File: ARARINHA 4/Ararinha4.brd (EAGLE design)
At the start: 160 x 100 mm, 105 parts, among them IC1 4053N, Q1 BC548, Q2 BC548, Q3 BC548, Q4 BC548, Q5 BC548, Q6 BC548, U1 LM386

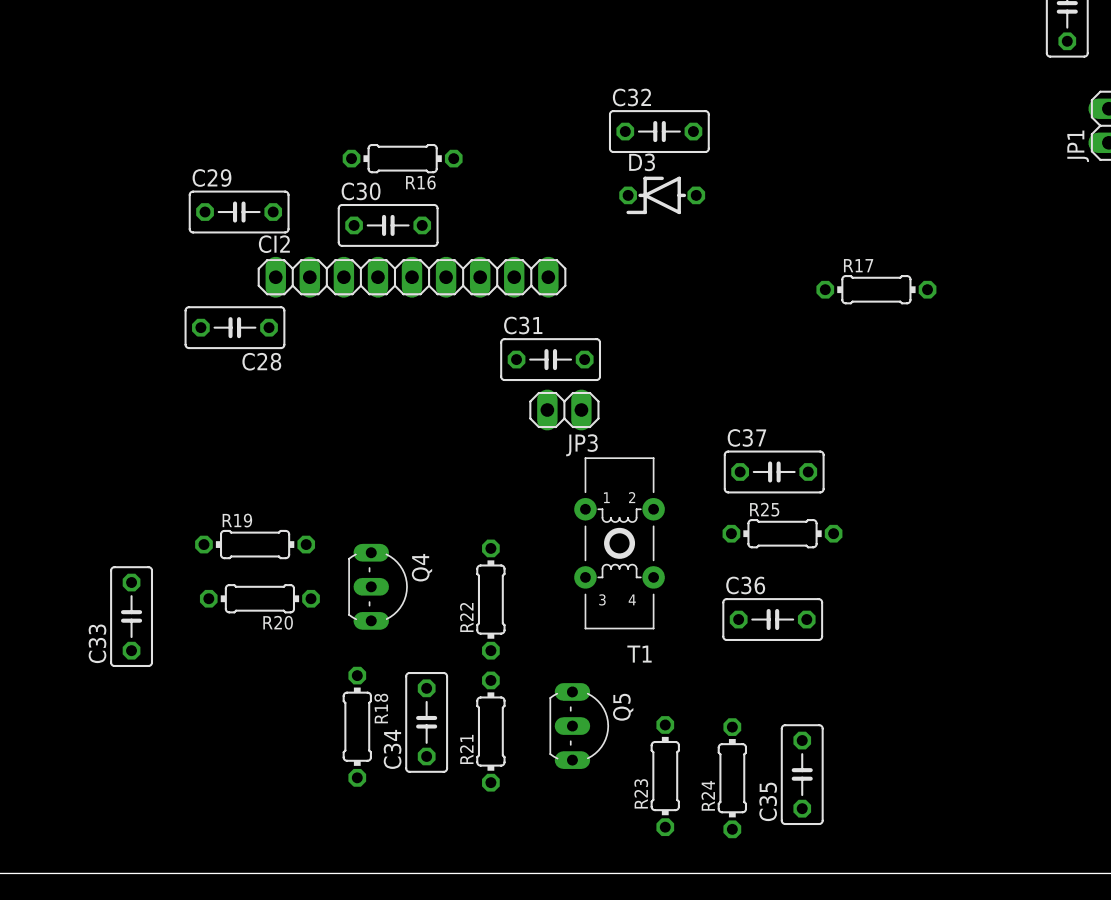
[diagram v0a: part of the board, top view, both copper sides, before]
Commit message: 
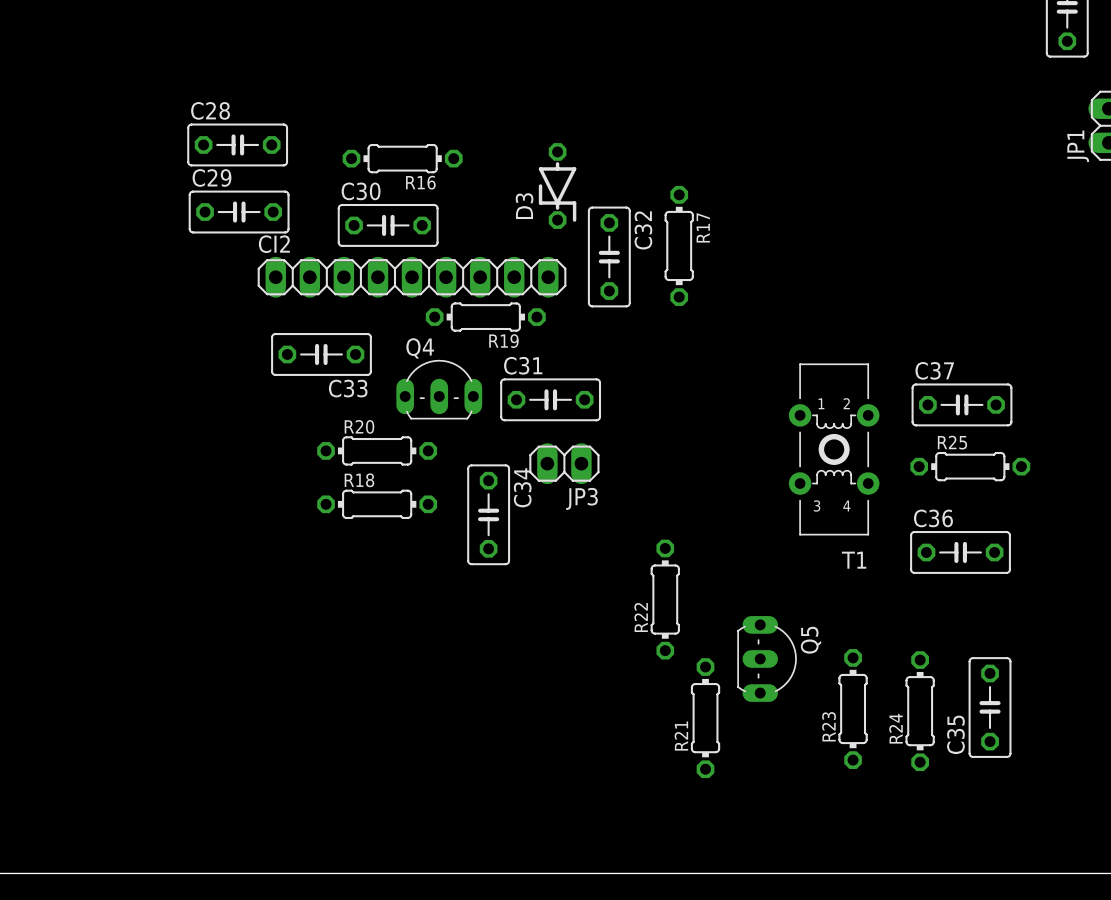
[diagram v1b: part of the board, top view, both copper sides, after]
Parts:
- moved R19 24.2 mm to (84.1, 41.5), turned to 180 degrees
- moved C33 24.1 mm to (71.8, 38.7), turned to 180 degrees
- moved T1 17.5 mm to (110.1, 31.6)
- moved R18 16.6 mm to (76.0, 27.5), turned to 0 degrees
- moved C34 16.2 mm to (84.3, 26.7), turned to 270 degrees
- moved R21 16.0 mm to (100.5, 11.6)
- moved Q4 15.9 mm to (80.6, 36.8), turned to 0 degrees
- moved R17 15.1 mm to (98.5, 46.8), turned to 270 degrees
- moved C35 14.9 mm to (121.7, 12.4)
- moved C36 14.9 mm to (119.5, 23.9)
- moved C37 14.9 mm to (119.6, 34.9)
- moved Q5 14.9 mm to (105.8, 16.0)
- moved R23 14.9 mm to (111.5, 12.3)
- moved R24 14.9 mm to (116.5, 12.1)
- moved R25 14.9 mm to (120.2, 30.3)
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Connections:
- net GND: now also C28.1, R18.1; no longer C28.2, R18.2
- net N$30: now also C28.2; no longer C28.1
- net N$41: now also R18.2; no longer R18.1
- net N$42: now also R20.2; no longer R20.1
- net N$44: now also R20.1; no longer R20.2

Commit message: 
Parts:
- added RXANT: TXOUT, pinhead:1X02
- moved T2 199.5 mm to (96.6, 30.8), turned to 270 degrees
- moved R30 183.5 mm to (102.0, 32.7), turned to 270 degrees
- moved R32 169.0 mm to (62.8, 26.0), turned to 270 degrees
- moved C16 167.1 mm to (68.4, 68.1), turned to 90 degrees
- moved C41 158.2 mm to (88.4, 22.7), turned to 270 degrees
- moved C40 157.9 mm to (96.8, 22.4), turned to 180 degrees
- moved R29 156.0 mm to (80.0, 28.3)
- moved JP5 148.4 mm to (104.7, 21.8), turned to 270 degrees
- moved R28 145.3 mm to (80.0, 32.0)
- moved Q6 142.8 mm to (88.1, 32.6), turned to 180 degrees
- moved C23 139.4 mm to (72.7, 20.0), turned to 270 degrees
- moved R31 135.4 mm to (46.2, 48.2), turned to 180 degrees
- moved R27 134.5 mm to (80.0, 35.9)
- moved C39 134.0 mm to (80.7, 23.7), turned to 180 degrees
- moved JP4 132.2 mm to (32.2, 31.3), turned to 90 degrees
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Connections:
- removed net N$13 (its old number): C6.2, R7.3
- new net N$10: C6.1, R7.1
- net GND: now also C15.1, C35.1, R21.2, R7.3, RXANT.1; no longer C15.2, C35.2, R21.1, R7.1
- net N$14: now also C6.2; no longer C6.1
- net N$21: now also C15.2; no longer C15.1
- net N$43: now also C35.2; no longer C35.1
- net N$46: now also R21.1; no longer R21.2
- net RXANT: now also RXANT.2
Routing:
- net GND: track 32.9 -> 541.0 mm
- net RX: track 0.00 -> 137.3 mm
- net N$24: track 0.00 -> 105.3 mm
- net VCC: track 0.00 -> 85.4 mm
- net N$23: track 0.00 -> 65.8 mm
- net TX: track 0.00 -> 43.3 mm
- net CRYSTALFILTEROUT3: track 0.00 -> 40.2 mm
- net BPF_IN: track 0.00 -> 38.1 mm
- net N$38: track 0.00 -> 31.2 mm
- net N$8: track 0.00 -> 31.2 mm
- net N$49: track 0.00 -> 27.0 mm
- net CRYSTALFILTEROUT: track 0.00 -> 26.8 mm
- net BPF: track 0.00 -> 26.4 mm
- net N$9: track 0.00 -> 25.0 mm
- net CRYSTALFILTERIN: track 0.00 -> 23.1 mm
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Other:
- board size 160 x 100 mm -> 108.5 x 100.5 mm
